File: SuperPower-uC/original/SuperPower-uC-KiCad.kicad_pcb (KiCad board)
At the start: 2 copper layers, 147 parts, among them J1 JST_PH_S2B_thru, J2 Barrel_Jack_Switch, J3 Conn_01x02_Male, J4 DNP/JST_ZH_S2B_thru, J5 JST_XH_S2B_thru, J6 Conn_01x02_Male, J7 mcu_pinout, J8 mcu_pinout, Q1 DMN2019UTS, Q10 2N7002A, Q11 2N7002A, Q12 DMP2035UVT, Q13 DMP2035UVT, Q14 DMP2035UVT, Q2 DMP3028LSD, Q3 DMN3018SSD, Q4 2N7002A, Q5 DMP2035UVT, Q6 BSS84-7-F, Q7 S8050, Q8 S8050, Q9 2N7002A, SW1 DNP/SKRKAEE020, U1 AP9101CK6-AYTRG1, U10 TPS63070RNMT, U2 USB-C, U3 IP4220CZ6, U4 LTC4162EUFD-LAD, U5 RV-3028-C7, U6 CP2102N-A01-GQFN28, U7 ESP32-WROOM32, U8 TPS70933DRVT, U9 TPS63070RNMT

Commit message: Update Placement + Increase MTG Hole Size
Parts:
- removed the R33 at (125.6, 92.8)
- removed e: TestPoint, TestPoint:TestPoint_Pad_D1.0mm
- added R6: 5.1k, Resistor_SMD:R_0603_1608Metric, F.Cu at (119.6, 56.9)
- added TP1: BATT+, TestPoint:TestPoint_Pad_D1.0mm, F.Cu at (183.4, 73.7)
- added TP10: 3V3_I2C, TestPoint:TestPoint_Pad_D1.0mm, F.Cu at (189.9, 73.5)
- added TP11: SCL, TestPoint:TestPoint_Pad_D1.0mm, F.Cu at (189.9, 76.6)
- added TP12: SDA, TestPoint:TestPoint_Pad_D1.0mm, F.Cu at (192.9, 73.5)
- added TP13: ~SMBALERT, TestPoint:TestPoint_Pad_D1.0mm, F.Cu at (192.9, 76.6)
- added TP18: TestPoint, TestPoint:TestPoint_Pad_D1.0mm, F.Cu at (165.4, 76.3)
- added TP19: TestPoint, TestPoint:TestPoint_Pad_D1.0mm, F.Cu at (176.1, 76.6)
- added TP2: BATT-, TestPoint:TestPoint_Pad_D1.0mm, F.Cu at (177.3, 73.7)
- added TP20: TestPoint, TestPoint:TestPoint_Pad_D1.0mm, F.Cu at (165.4, 73.3)
- added TP21: TestPoint, TestPoint:TestPoint_Pad_D1.0mm, F.Cu at (162.4, 76.3)
- added TP22: TestPoint, TestPoint:TestPoint_Pad_D1.0mm, F.Cu at (173.1, 76.6)
- added TP23: TestPoint, TestPoint:TestPoint_Pad_D1.0mm, F.Cu at (162.4, 73.3)
- added TP24: TestPoint, TestPoint:TestPoint_Pad_D1.0mm, F.Cu at (159.3, 76.3)
- added TP25: TestPoint, TestPoint:TestPoint_Pad_D1.0mm, F.Cu at (170.0, 76.6)
- added TP26: TestPoint, TestPoint:TestPoint_Pad_D1.0mm, F.Cu at (159.3, 73.3)
- added TP27: TestPoint, TestPoint:TestPoint_Pad_D1.0mm, F.Cu at (156.3, 76.3)
- added TP28: TestPoint, TestPoint:TestPoint_Pad_D1.0mm, F.Cu at (156.3, 73.3)
- added TP3: GND, TestPoint:TestPoint_Pad_D1.0mm, F.Cu at (180.4, 73.7)
- added TP6: TestPoint, TestPoint:TestPoint_Pad_D1.0mm, F.Cu at (128.7, 55.5)
- added TP8: CHARGER_VIN, TestPoint:TestPoint_Pad_D1.0mm, F.Cu at (186.8, 73.5)
- added TP9: VOUT, TestPoint:TestPoint_Pad_D1.0mm, F.Cu at (186.8, 76.6)
- H1, H3: footprint MountingHole:MountingHole_2.2mm_M2_Pad_Via -> MountingHole:MountingHole_2.7mm_M2.5_Pad_Via
- H2, H4: footprint MountingHole:MountingHole_2.2mm_M2_Pad_Via -> MountingHole:MountingHole_2.7mm_Pad_Via
- JP1, JP3: moved to B.Cu
- R33: renamed from R6; value 5.1k -> 470
- moved J4 109.2 mm to (140.0, 34.0), turned to 180 degrees
- moved D3 109.1 mm to (192.5, 34.2)
- moved J1 103.2 mm to (134.8, 36.0), turned to 180 degrees
- moved C9 102.6 mm to (192.8, 38.5), turned to 0 degrees
- moved U7 92.3 mm to (195.2, 55.0)
- moved J8 91.9 mm to (203.0, 67.2)
- moved J7 91.3 mm to (160.0, 43.0)
- moved JP2 88.1 mm to (147.5, 65.8), turned to 180 degrees
- moved J5 86.5 mm to (117.2, 41.0)
- moved R11 84.5 mm to (171.5, 60.8)
- moved R26 84.5 mm to (171.5, 62.3)
- moved R39 84.5 mm to (171.5, 63.9)
- moved Q13 84.5 mm to (174.8, 62.7)
- moved Q9 84.5 mm to (174.8, 59.0)
- moved JP3 81.6 mm to (159.0, 35.2)
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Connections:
- R33 pad 1: Net-(R6-Pad1) -> /MCU Module/TXD
- R33 pad 2: GND -> Net-(R33-Pad2)
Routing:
- net /Charging Module/3v3_I2C: track 32.3 -> 2.94 mm, vias 4 -> 2
- net /SCL: track 25.8 -> 0.89 mm, vias 2 -> 0
- net /SDA: track 22.3 -> 0.00 mm
- net /RTC/EVI: track 19.4 -> 0.00 mm
- net /RTC/~INT: track 19.7 -> 3.95 mm, vias 2 -> 0
- net /Charger inputs and USB IO/V_CHARGE: track 30.3 -> 22.9 mm
- net VDD: track 17.6 -> 13.6 mm
- net GND: track 31.1 -> 28.6 mm, vias 6 -> 0
- net /MCU Module/3v3_MCU: track 8.27 -> 5.95 mm
- net Net-(R24-Pad2): track 1.76 -> 0.00 mm
- net /RTC/VIN: track 1.57 -> 0.00 mm
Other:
- board outline added: 95 x 50 mm

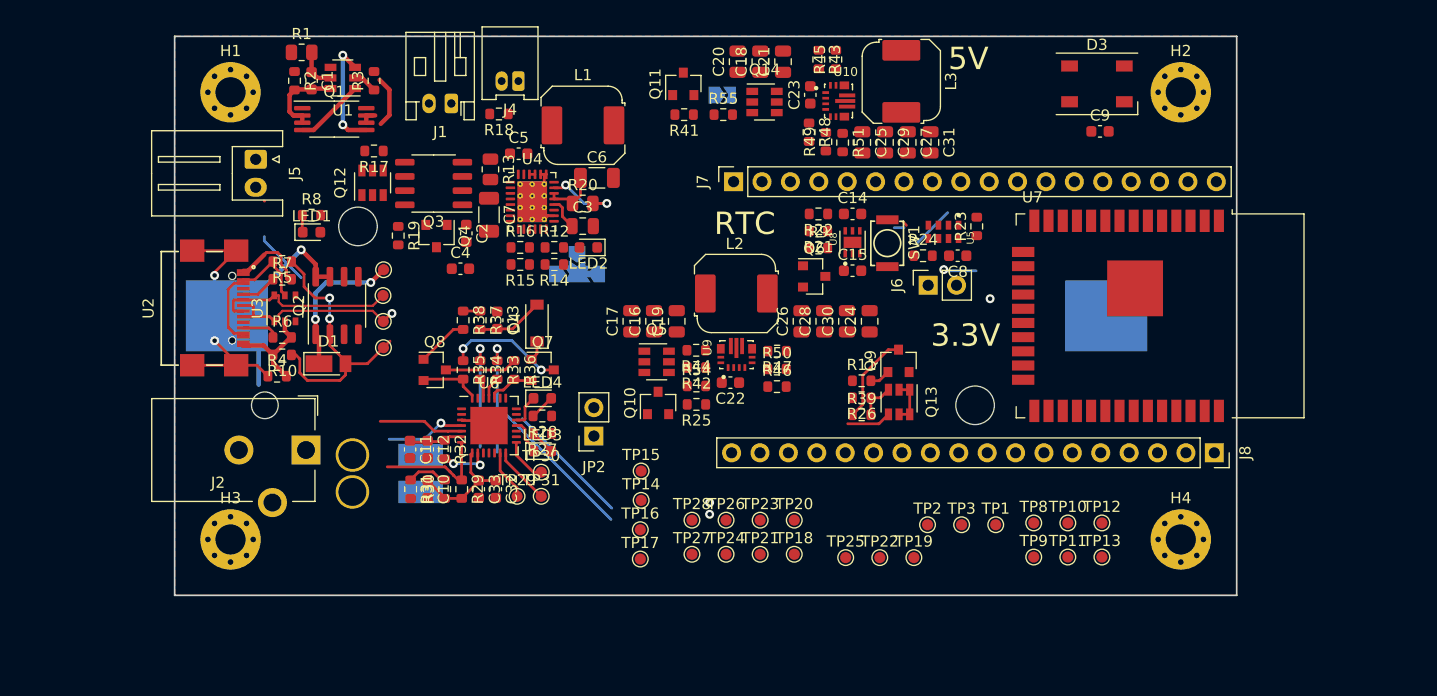
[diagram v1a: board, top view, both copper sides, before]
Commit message: Shrink board height + Add Coin cell holder
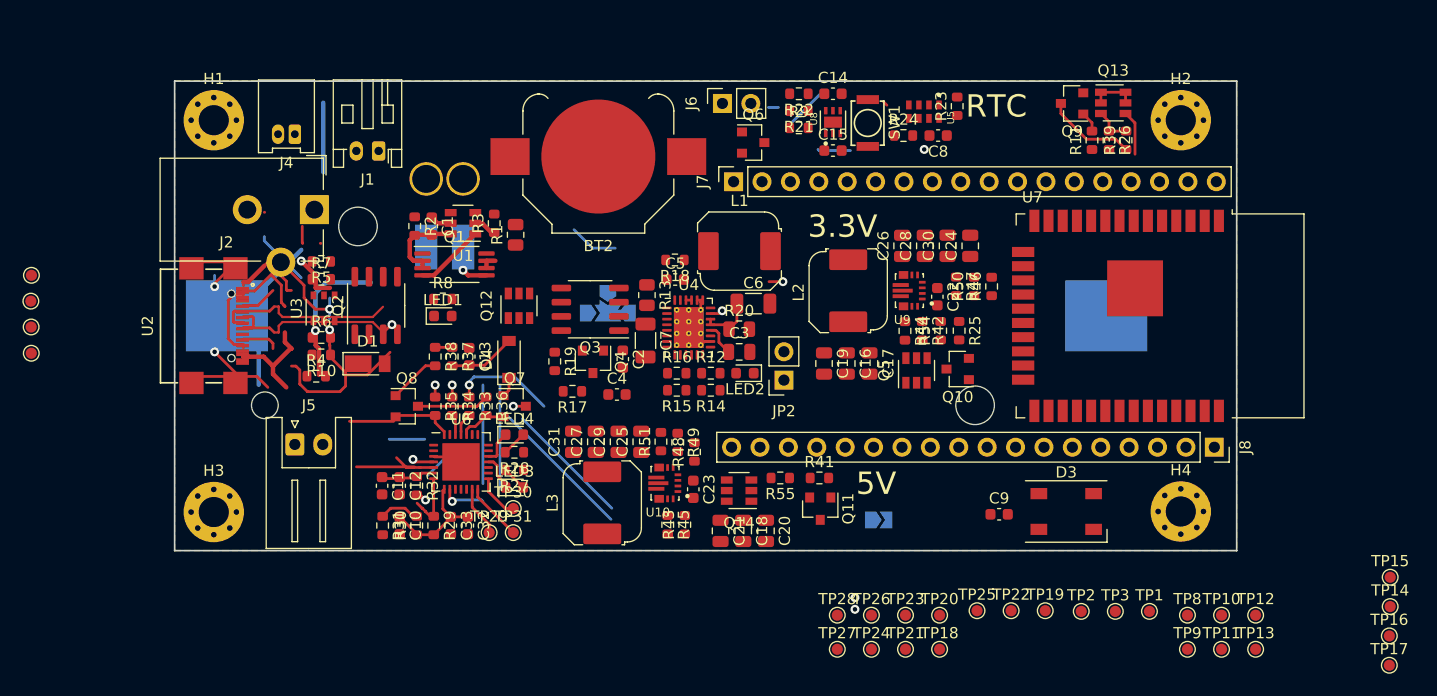
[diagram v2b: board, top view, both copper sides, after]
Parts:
- added BT2: Battery_Cell, Battery:BatteryHolder_Keystone_3000_1x12mm, F.Cu at (147.9, 40.8)
- moved TP14 67.7 mm to (218.7, 81.0)
- moved TP15 67.7 mm to (218.7, 78.4)
- moved TP16 67.7 mm to (218.7, 83.6)
- moved TP17 67.7 mm to (218.7, 86.3)
- moved L3 46.2 mm to (148.2, 71.7), turned to 270 degrees
- moved R45 44.2 mm to (154.1, 73.7), turned to 270 degrees
- moved R43 43.3 mm to (155.6, 73.7), turned to 90 degrees
- moved C21 42.3 mm to (158.8, 74.2), turned to 270 degrees
- moved C20 42.0 mm to (162.9, 74.2), turned to 270 degrees
- moved C18 42.0 mm to (160.9, 74.2), turned to 270 degrees
- moved C31 41.7 mm to (145.6, 66.3), turned to 90 degrees
- moved JP3 40.5 mm to (173.0, 73.2)
- moved Q11 39.9 mm to (167.8, 72.2), turned to 270 degrees
- moved C27 38.7 mm to (147.7, 66.3), turned to 90 degrees
- moved D3 38.3 mm to (189.8, 72.5)
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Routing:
- net GND: track 28.6 -> 13.8 mm
- net VBUS: track 14.2 -> 24.4 mm
- net Net-(Q7-Pad3): track 10.6 -> 2.21 mm
- net /MCU Module/TXD: track 21.7 -> 30.0 mm
- net /VBUS1: track 35.0 -> 29.8 mm
- net /Charger inputs and USB IO/V_CHARGE: track 22.9 -> 18.7 mm, vias 1 -> 0
- net /MCU Module/DTR: track 5.38 -> 9.33 mm
- net Net-(U2-PadA8): track 0.00 -> 3.29 mm
- net Net-(R6-Pad1): track 3.29 -> 0.00 mm
- net Net-(U2-PadB8): track 0.00 -> 3.21 mm
- net Net-(C1-Pad1): track 3.68 -> 1.91 mm
- net VDD: track 13.6 -> 12.0 mm, vias 2 -> 1
- net Net-(Q1-Pad5): track 10.1 -> 8.52 mm, vias 2 -> 1
- net /D-: track 24.1 -> 25.3 mm
- net Net-(R7-Pad1): track 3.21 -> 4.21 mm, vias 0 -> 1
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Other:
- board size 95 x 50 mm -> 95 x 42 mm

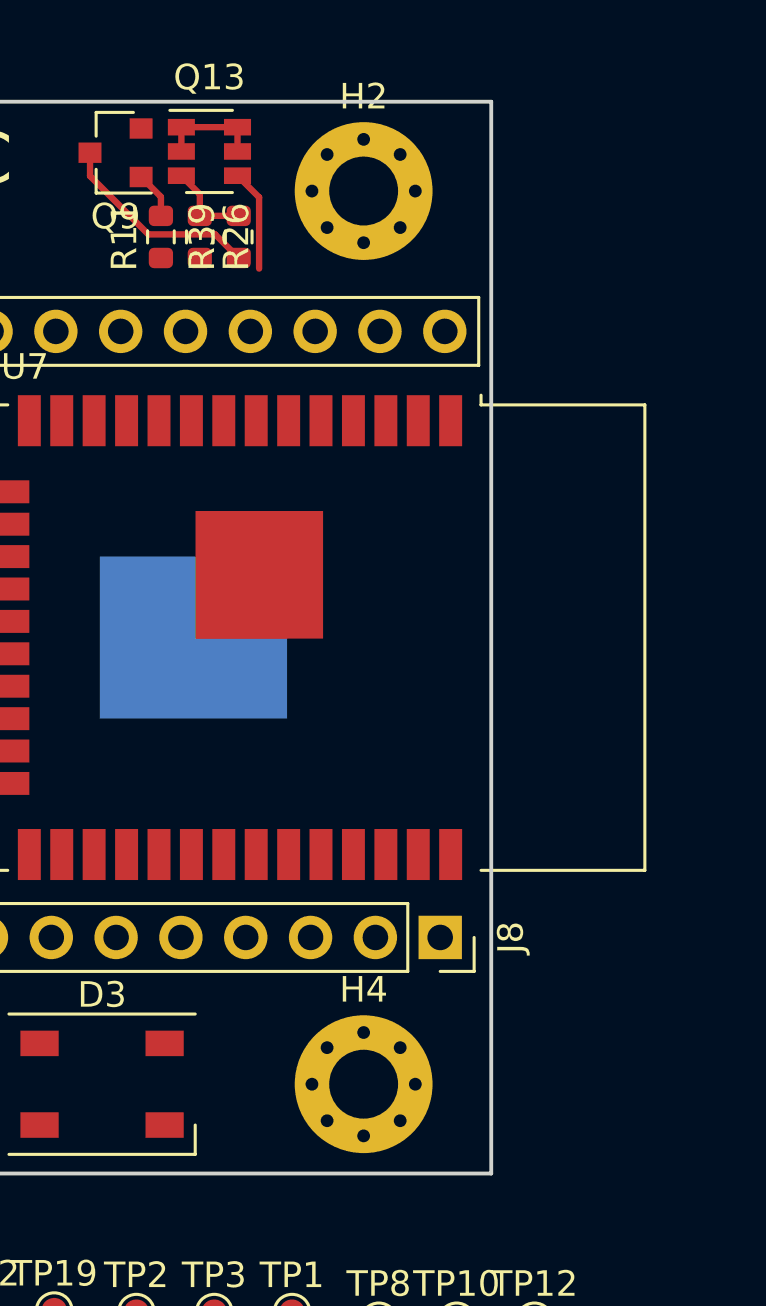
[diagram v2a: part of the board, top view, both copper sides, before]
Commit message: Convert 3D Board into Step + Draw a simple Box
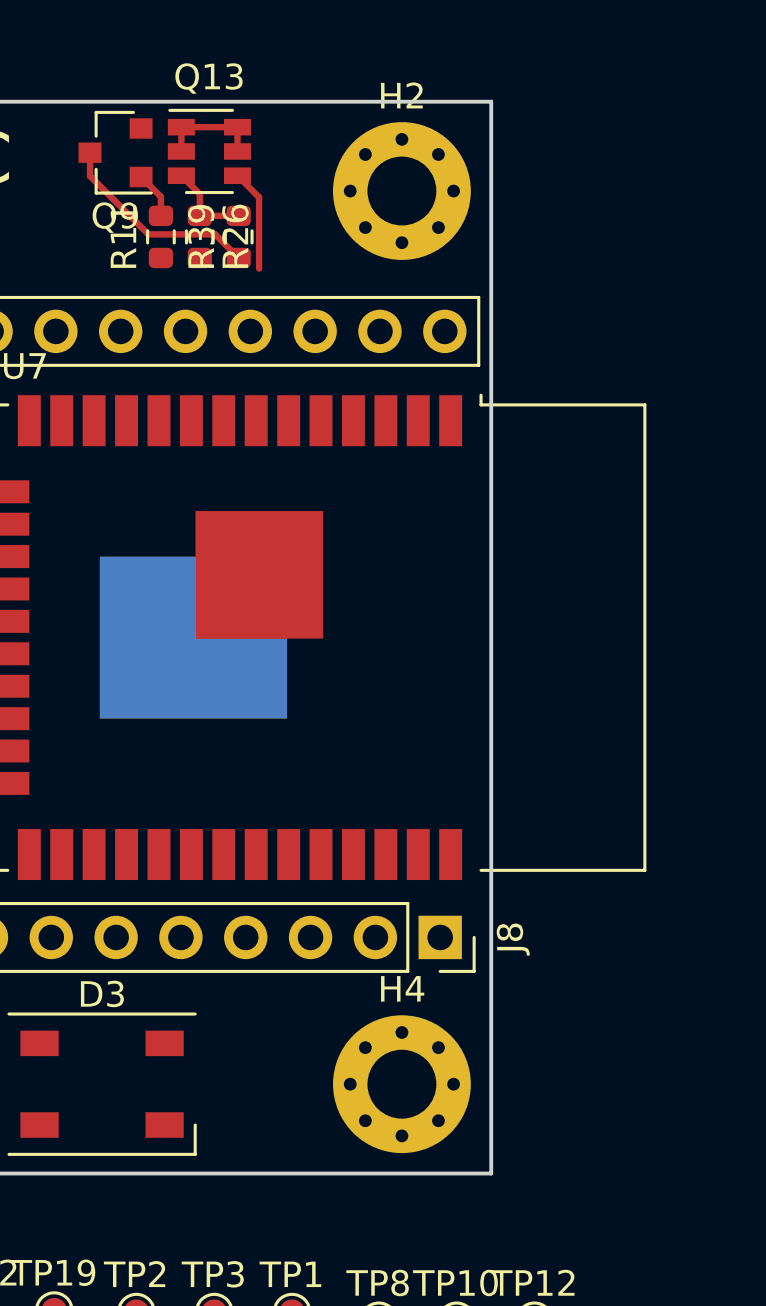
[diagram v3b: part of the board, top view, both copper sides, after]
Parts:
- moved H2 1.50 mm to (201.5, 37.5)
- moved H4 1.50 mm to (201.5, 72.5)

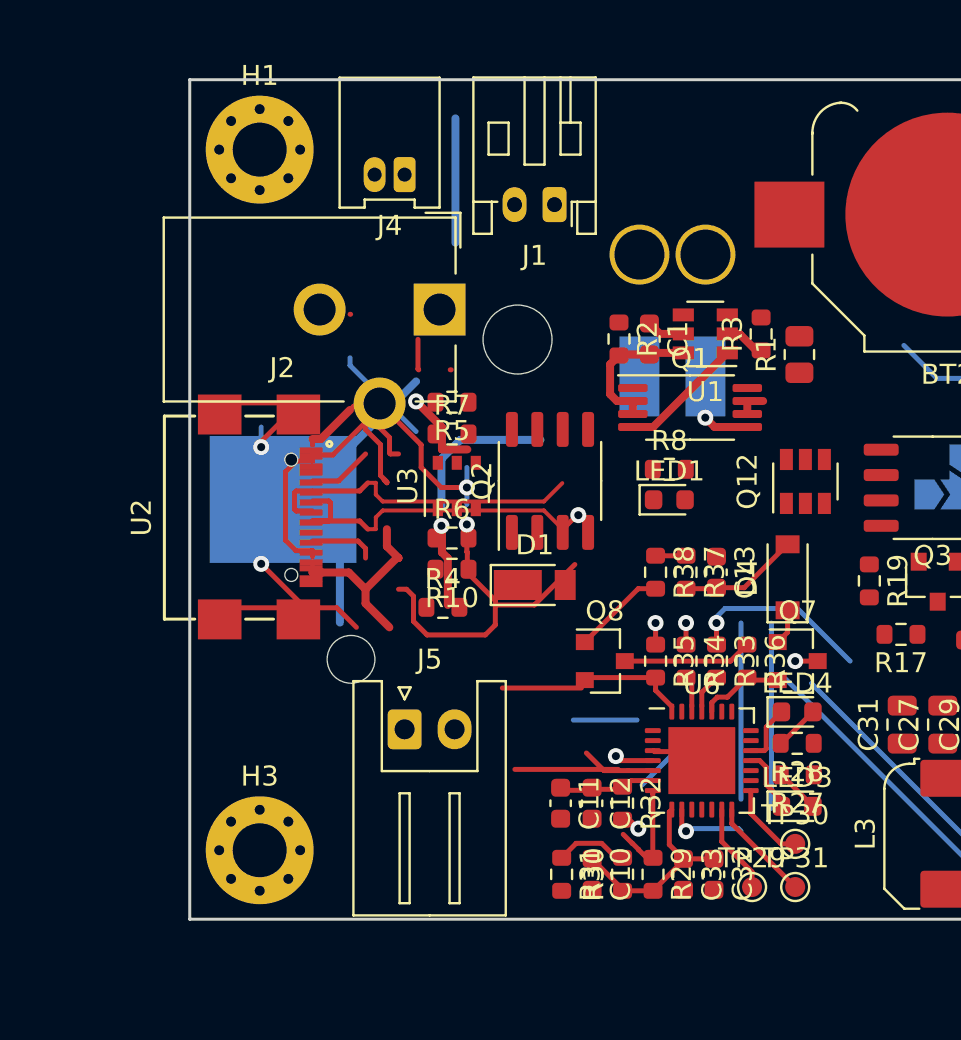
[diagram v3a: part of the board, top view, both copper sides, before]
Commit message: Make all connectors on only 2 sides.
+ Move DC Jack Connector to avoid having pads in conflict with the battery holder body.
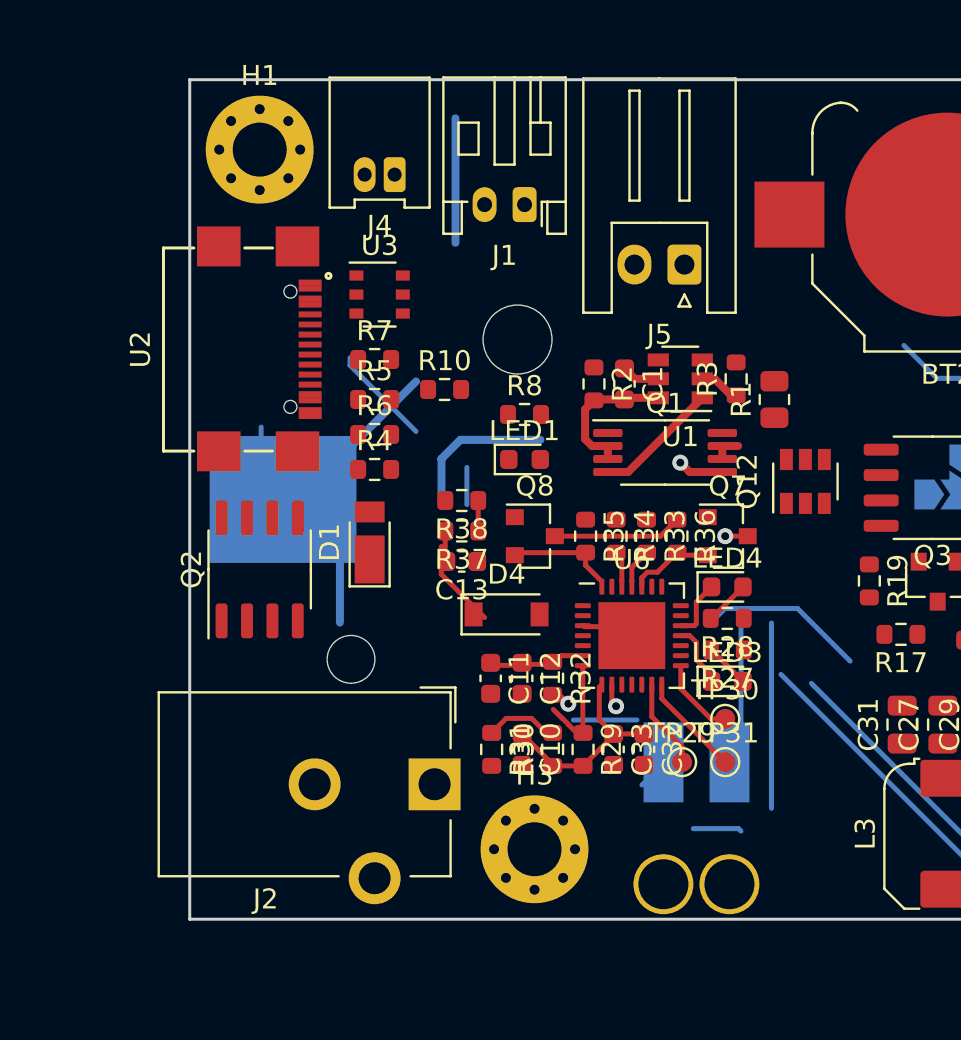
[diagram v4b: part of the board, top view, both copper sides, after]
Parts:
- moved J5 27.1 mm to (134.8, 43.2), turned to 180 degrees
- moved J2 23.8 mm to (122.2, 69.2)
- moved J3 23.4 mm to (135.3, 70.2), turned to 180 degrees
- moved Q2 15.2 mm to (113.5, 58.5)
- moved D4 14.2 mm to (125.8, 60.8), turned to 0 degrees
- moved H3 13.8 mm to (127.2, 72.5)
- moved C13 12.8 mm to (123.6, 58.1), turned to 180 degrees
- moved R37 11.4 mm to (123.6, 56.6), turned to 180 degrees
- moved R38 10.3 mm to (123.6, 55.1), turned to 180 degrees
- moved U3 10.3 mm to (119.5, 44.8), turned to 0 degrees
- moved R10 9.00 mm to (122.8, 49.5), turned to 0 degrees
- moved D1 8.53 mm to (119.0, 57.1), turned to 90 degrees
- moved U2 8.41 mm to (112.8, 47.5)
- moved R8 7.74 mm to (126.8, 50.8)
- moved R4 7.70 mm to (119.2, 53.5)
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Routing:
- net /D-: track 25.3 -> 0.00 mm
- net /D+: track 24.7 -> 0.00 mm, vias 2 -> 0
- net VBUS: track 24.4 -> 0.00 mm
- net Net-(R4-Pad1): track 23.0 -> 0.00 mm, vias 2 -> 0
- net /VBUS1: track 29.8 -> 7.20 mm, vias 2 -> 0
- net +BATT: track 4.90 -> 24.4 mm
- net /MCU Module/RXD: track 23.3 -> 13.4 mm, vias 2 -> 1
- net /Charger inputs and USB IO/V_CHARGE: track 18.7 -> 13.9 mm
- net /MCU Module/IO0: track 4.65 -> 0.00 mm
- net Net-(R7-Pad1): track 4.21 -> 0.00 mm, vias 1 -> 0
- net VDD: track 12.0 -> 7.83 mm, vias 1 -> 0
- net /MCU Module/DTR: track 9.33 -> 5.38 mm
- net Net-(U2-PadA8): track 3.29 -> 0.00 mm
- net Net-(U2-PadB8): track 3.21 -> 0.00 mm
- net GND: track 13.8 -> 11.8 mm
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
